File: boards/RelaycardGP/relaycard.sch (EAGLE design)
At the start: 33 parts, among them IC1 ULN2801A, K3 NA, K4 NA, K5 NA, K6 NA, K7 NA, X1 112404, X15 112404, X16 112404, X2 112404, X3 112404, X4 112404, X5 112404, X6 112404, X7 112404, X8 112404

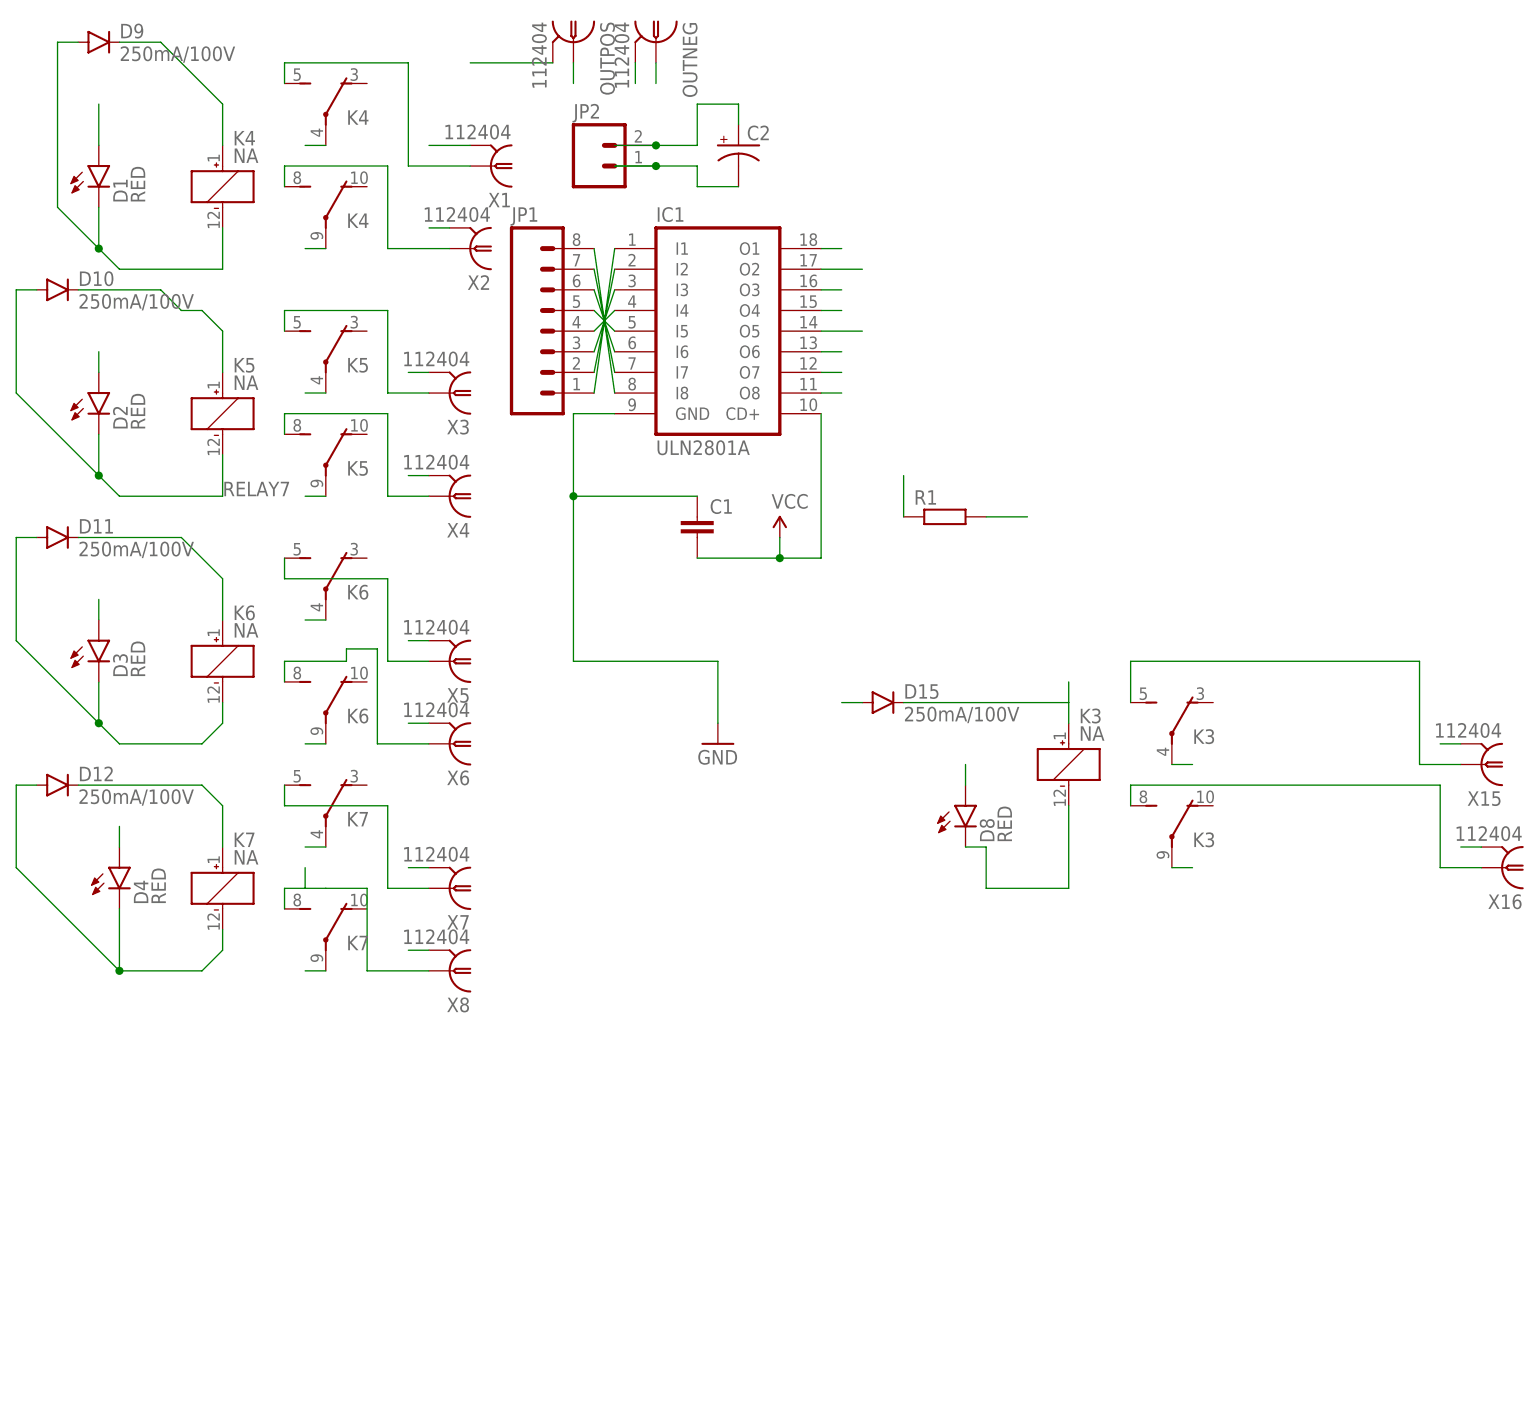
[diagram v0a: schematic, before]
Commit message: Allow to remove methods
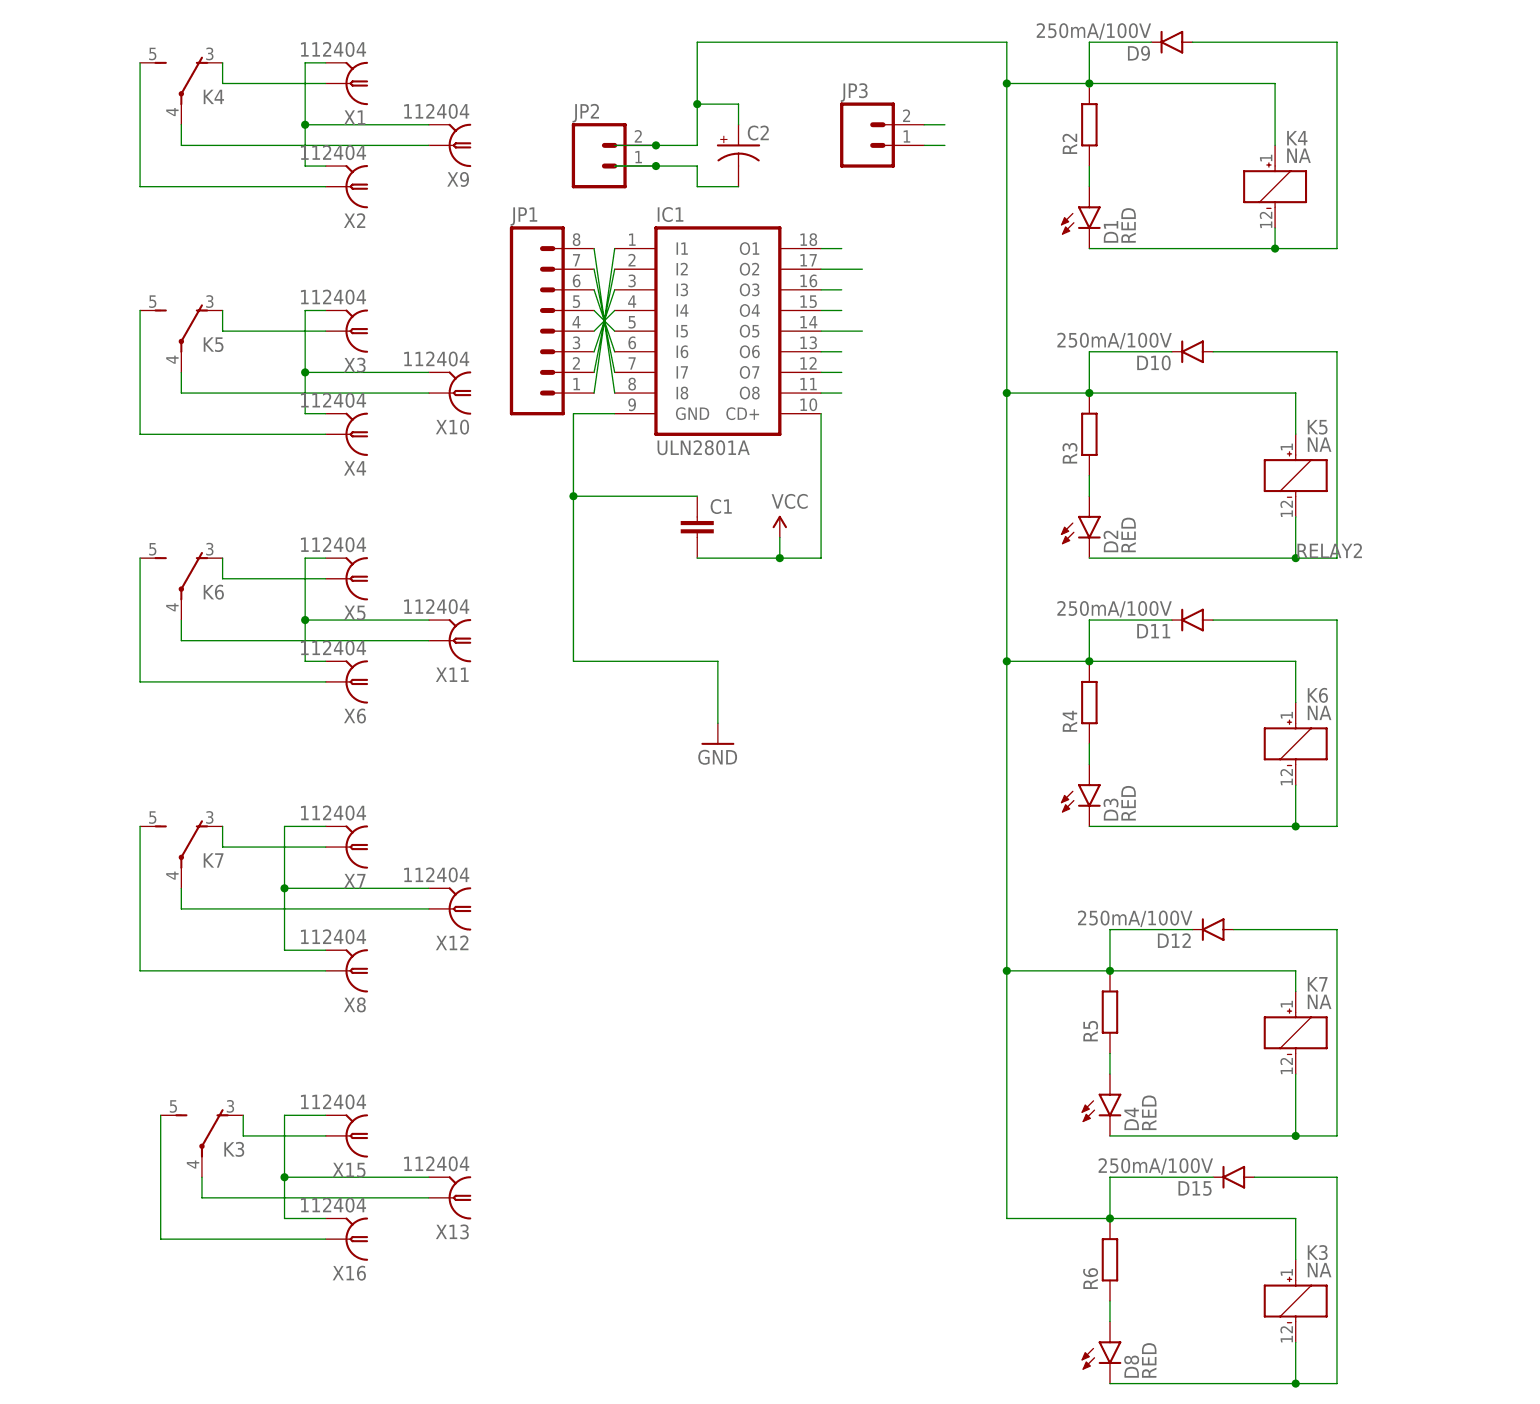
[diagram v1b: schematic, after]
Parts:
- removed OUTNEG, OUTPOS: 112404, amphenol-112404_10:112404
- removed R1: (no value), resistor:R-EU_R1206W
- added JP3: (no value), SparkFun-Connectors:M02PTH
- added R2, R3, R4, R5, R6: (no value), resistor:R-EU_R1206W
- added X10, X11, X12, X13, X9: 112404, amphenol-112404_10:112404
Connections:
- removed net GND: C1.1, C2.-, IC1.GND, JP2.1, OUTNEG.2, OUTPOS.2, X1.2, X15.2, X16.2, X2.2, X3.2, X4.2, X5.2, X6.2, X7.2, X8.2
- removed net N$24: K32.S, X15.1
- removed net N$25: K33.S, X16.1
- removed net OUTNEG: K33.P, K43.P, K53.P, K63.P, K73.P, OUTNEG.1
- removed net OUTPOS: K32.P, K42.P, K52.P, K62.P, K72.P, OUTPOS.1
- removed net RELAY_8: D1.C, D9.A, IC1.O6, K41.-
- removed net RES: D1.A, D2.A, D3.A, D4.A, D8.A, R1.2
- new net A: D1.A, R2.1
- new net B: D2.A, R3.1
- new net C: D3.A, R4.1
- new net D: D4.A, R5.1
- new net E: D8.A, R6.1
- new net GND1: X1.2, X2.2, X9.2
- new net GND2: X10.2, X3.2, X4.2
- new net GND3: X11.2, X5.2, X6.2
- new net GND4: X12.2, X7.2, X8.2
- new net GND5: X13.2, X15.2, X16.2
- new net GND_V: C1.1, C2.-, IC1.GND, JP2.1, JP3.1, JP3.2
- new net N$15: K62.S, X6.1
- new net N$16: K62.P, X11.1
- new net N$17: K72.O, X7.1
- new net N$19: K72.S, X8.1
- new net N$20: K72.P, X12.1
- new net N$22: K32.S, X16.1
- new net RELAY5: D15.A, D8.C, IC1.O1, K31.-
- net N$1: now also X2.1; no longer X1.1
- net N$13: now also K52.P, X10.1; no longer D15.C, K31.+
- net N$14: now also K62.O, X5.1; no longer K63.S, X6.1
- net N$21: now also K32.O, X15.1; no longer K72.S, X7.1
- net N$23: now also K32.P, X13.1; no longer K73.S, X8.1
- net N$3: now also K42.O, X1.1; no longer K43.S, X2.1
- net N$4: now also K42.P, X9.1; no longer K52.S, X3.1
- net N$5: now also K52.S; no longer K53.S
- net N$7: now also K52.O, X3.1; no longer K62.S, X5.1
- net RELAY1: now also D1.C, D9.A, K41.-
- net RELAY2: now also D10.A, D2.C, IC1.O3, K51.-; no longer IC1.O1
- net RELAY3: now also D11.A, D3.C, IC1.O4, K61.-; no longer IC1.O8
- net RELAY4: now also D12.A, D4.C, IC1.O5, K71.-; no longer D15.A, D8.C, IC1.O7, K31.-
- net RELAY6: now also IC1.O6; no longer D11.A, D3.C, IC1.O4, K61.-
- net RELAY7: now also IC1.O7; no longer D10.A, D2.C, IC1.O5, K51.-
- net RELAY8: now also IC1.O8; no longer D12.A, D4.C, IC1.O3, K71.-
- net VCC: now also D15.C, K31.+, R2.2, R3.2, R4.2, R5.2, R6.2; no longer R1.1
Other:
- moved on the sheet: D1, D10, D11, D12, D15, D2, D3, D4, D8, D9, K3, K4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
